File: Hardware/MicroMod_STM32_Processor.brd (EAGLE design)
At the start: 22 x 22 mm, 47 parts, among them J1 MICROMOD-2222, U1 STM32F405RGT6, U3 W25QXX128MBIT-6X5, Y1 12MHz, Y2 32.768kHz

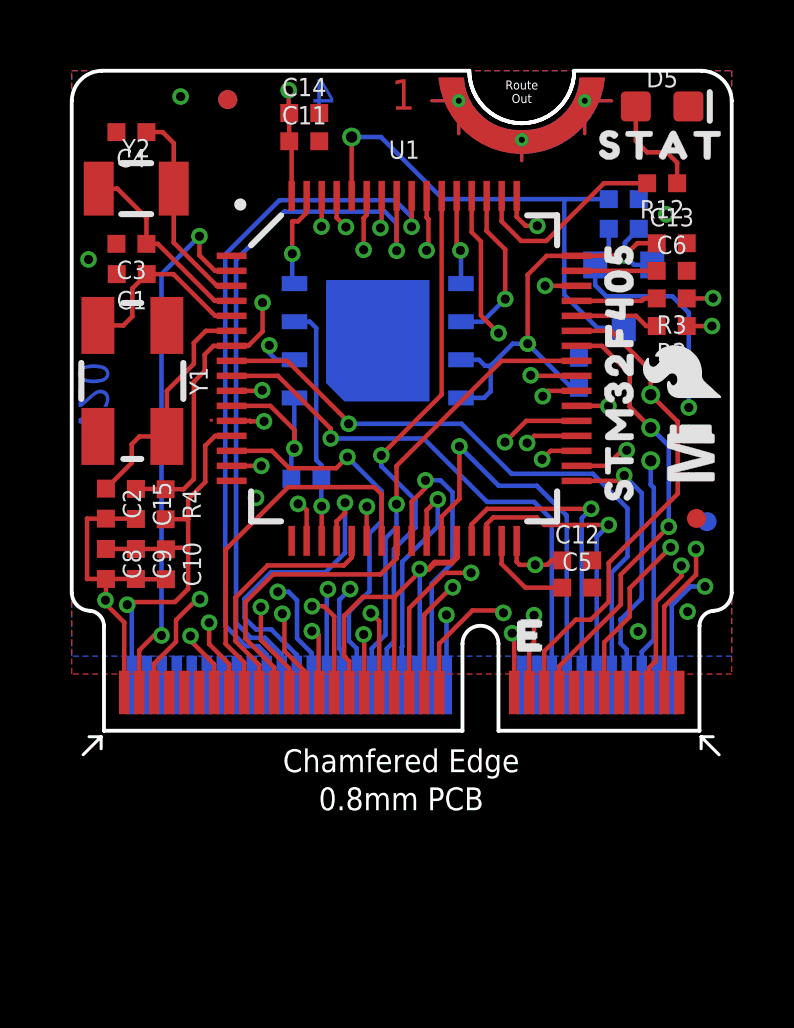
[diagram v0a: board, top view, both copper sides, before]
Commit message: Move some vias, replace STM32 with library part.
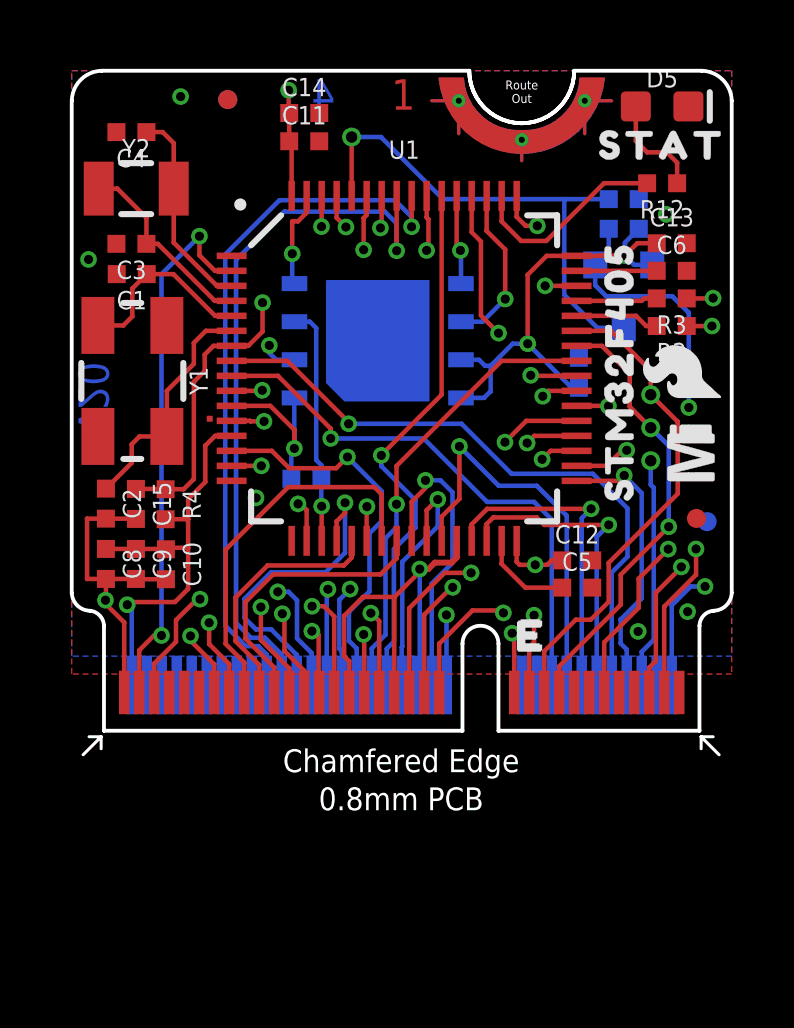
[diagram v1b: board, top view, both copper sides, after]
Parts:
- U1: device STM32_Temp:TQFP64 -> SparkFun-IC-Microcontroller:TQFP64
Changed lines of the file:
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@@
 <dimension x1="0" y1="21" x2="22" y2="21" x3="11" y3="26" textsize="1.27" textratio="15" layer="47" visible="yes"/>
 <text x="-3.454" y="-16.074" size="1.778" layer="51" font="vector">Revised by: Alex Brudner</text>
-<rectangle x1="4.6" y1="10.3" x2="4.7" y2="10.4" layer="1"/>
+<rectangle x1="4.5" y1="10.3" x2="4.7" y2="10.5" layer="1"/>
 <rectangle x1="7" y1="6.3" x2="7.1" y2="6.4" layer="41"/>
 <rectangle x1="6.9" y1="7.1" x2="7" y2="7.5" layer="41"/>
@@
 <attribute name="VALUE" x="2.568" y="7.55" size="0.6096" layer="27" font="vector" ratio="20" rot="R270" align="top-center"/>
 </element>
-<element name="U1" library="STM32_Temp" package="TQFP64" value="STM32F405RGT6" x="11.08" y="12.08" smashed="yes" rot="R270">
+<element name="U1" library="SparkFun-IC-Microcontroller" package="TQFP64" value="STM32F405RGT6" x="11.08" y="12.08" smashed="yes" rot="R270">
 <attribute name="NAME" x="11.08" y="19.065" size="0.6096" layer="25" font="vector" ratio="20" align="bottom-center"/>
 <attribute name="PROD_ID" value="IC-11709" x="3.46" y="-32.37" size="1.778" layer="27" rot="R270" display="off"/>
@@
 <wire x1="20.569" y1="13.931" x2="20.0168" y2="14.4832" width="0.1524" layer="16"/>
 <wire x1="17.75" y1="1.275" x2="17.75" y2="2.95" width="0.1524" layer="1"/>
-<wire x1="17.75" y1="2.95" x2="18.6" y2="3.8" width="0.1524" layer="1"/>
-<wire x1="18.6" y1="3.8" x2="18.6" y2="4.74986875" width="0.1524" layer="1"/>
-<wire x1="18.6" y1="4.74986875" x2="19.96433125" y2="6.1142" width="0.1524" layer="1"/>
-<via x="19.96433125" y="6.1142" extent="1-16" drill="0.3048"/>
-<wire x1="19.96433125" y1="6.1142" x2="20.569" y2="6.71886875" width="0.1524" layer="15"/>
-<wire x1="20.569" y1="6.71886875" x2="20.569" y2="10.773" width="0.1524" layer="15"/>
+<wire x1="17.75" y1="2.95" x2="18.9" y2="4.1" width="0.1524" layer="1"/>
+<wire x1="18.9" y1="4.1" x2="18.9" y2="5.06986875" width="0.1524" layer="1"/>
+<wire x1="18.9" y1="5.06986875" x2="19.88433125" y2="6.0542" width="0.1524" layer="1"/>
+<via x="19.88433125" y="6.0542" extent="1-16" drill="0.3048"/>
+<wire x1="19.88433125" y1="6.0542" x2="20.569" y2="6.73886875" width="0.1524" layer="15"/>
+<wire x1="20.569" y1="6.73886875" x2="20.569" y2="10.773" width="0.1524" layer="15"/>
 </signal>
 <signal name="SCK">
@@
 <contactref element="R2" pad="1"/>
 <contactref element="J1" pad="5"/>
-<wire x1="19.47" y1="4.3" x2="19.47" y2="2.325" width="0.1524" layer="1"/>
+<wire x1="19.47" y1="4.6" x2="19.47" y2="2.325" width="0.1524" layer="1"/>
 <wire x1="19.25" y1="1.275" x2="19.25" y2="2.105" width="0.1524" layer="1"/>
 <wire x1="19.47" y1="2.325" x2="19.25" y2="2.105" width="0.1524" layer="1"/>
-<wire x1="20.32" y1="5.15" x2="20.32" y2="5.5" width="0.1524" layer="1"/>
-<wire x1="20.32" y1="5.15" x2="19.47" y2="4.3" width="0.1524" layer="1"/>
-<via x="20.32" y="5.5" extent="1-16" drill="0.3048"/>
-<wire x1="21.020425" y1="5.502" x2="21.458" y2="5.939575" width="0.1524" layer="2"/>
-<wire x1="21.020425" y1="5.502" x2="20.322" y2="5.502" width="0.1524" layer="2"/>
-<wire x1="20.32" y1="5.5" x2="20.322" y2="5.502" width="0.1524" layer="2"/>
+<wire x1="20.32" y1="5.45" x2="20.32" y2="5.46" width="0.1524" layer="1"/>
+<wire x1="20.32" y1="5.45" x2="19.47" y2="4.6" width="0.1524" layer="1"/>
+<via x="20.32" y="5.46" extent="1-16" drill="0.3048"/>
+<wire x1="20.980425" y1="5.462" x2="21.458" y2="5.939575" width="0.1524" layer="2"/>
+<wire x1="20.980425" y1="5.462" x2="20.322" y2="5.462" width="0.1524" layer="2"/>
+<wire x1="20.32" y1="5.46" x2="20.322" y2="5.462" width="0.1524" layer="2"/>
 <via x="21.34" y="13.49" extent="1-16" drill="0.3048"/>
 <wire x1="21.34" y1="13.49" x2="20.5" y2="13.49" width="0.1524" layer="1"/>

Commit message: Ready for v11 protos.
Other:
- board text added: "Board Thickness is 0.8mm 4-Layer Beveled Edge ENIG finish"
- board text added: "v11"
- board text removed: "0.8mm PCB ENIG finish 45 degree chamfered edge Four layer design"
- board text removed: "v20"
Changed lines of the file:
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@@
 <drawing>
 <settings>
-<setting alwaysvectorfont="yes"/>
+<setting alwaysvectorfont="no"/>
 <setting verticaltext="up"/>
 </settings>
@@
 <wire x1="0" y1="21" x2="1" y2="22" width="0.127" layer="20" curve="-87.205638"/>
 <wire x1="16.75" y1="22" x2="13.25" y2="22" width="0.127" layer="20" curve="-180"/>
-<text x="0.221" y="9.961" size="1.016" layer="16" font="vector" ratio="15" rot="SMR90">v20</text>
+<text x="0.221" y="9.961" size="1.016" layer="16" font="vector" ratio="15" rot="SMR90">v11</text>
 <text x="11.84" y="-12.98" size="1.778" layer="51" font="vector">Alex Wende</text>
-<text x="39" y="28" size="1.778" layer="51" font="vector" ratio="15">0.8mm PCB
-ENIG finish
-45 degree chamfered edge
-Four layer design</text>
+<text x="38.7" y="28.9" size="1.778" layer="51" font="vector" ratio="15">Board Thickness is 0.8mm
+4-Layer
+Beveled Edge
+ENIG finish</text>
 <text x="11.049" y="21.209" size="1.016" layer="1" font="vector" ratio="15" align="center">1</text>
 <text x="10.033" y="21.209" size="1.016" layer="2" font="vector" ratio="15" align="center">2</text>
@@
 <dimension x1="0" y1="21" x2="22" y2="21" x3="11" y3="26" textsize="1.27" textratio="15" layer="47" visible="yes"/>
 <text x="-3.454" y="-16.074" size="1.778" layer="51" font="vector">Revised by: Alex Brudner</text>
-<rectangle x1="4.5" y1="10.3" x2="4.7" y2="10.5" layer="1"/>
+<rectangle x1="4.5" y1="10.3" x2="4.7" y2="10.5" layer="41"/>
 <rectangle x1="7" y1="6.3" x2="7.1" y2="6.4" layer="41"/>
 <rectangle x1="6.9" y1="7.1" x2="7" y2="7.5" layer="41"/>
+<text x="39" y="31" size="1.778" layer="51" font="vector" ratio="15"></text>
+<text x="39" y="28" size="1.778" layer="51" font="vector" ratio="15"></text>
 </plain>
 <attributes>
@@
 <wire x1="16.83" y1="8.33" x2="18.236" y2="8.33" width="0.1524" layer="1"/>
 <contactref element="J1" pad="8"/>
-<wire x1="18.415" y1="8.509" x2="18.996" y2="7.928" width="0.1524" layer="16"/>
-<wire x1="18.996" y1="4.41" x2="18.996" y2="7.928" width="0.1524" layer="16"/>
+<wire x1="18.415" y1="8.509" x2="18.896" y2="8.028" width="0.1524" layer="16"/>
+<wire x1="18.896" y1="4.41" x2="18.896" y2="8.028" width="0.1524" layer="16"/>
 <wire x1="18.5" y1="1.525" x2="18.5" y2="2.7075" width="0.1524" layer="16"/>
 <wire x1="18.5" y1="2.7075" x2="18.2974" y2="2.9101" width="0.1524" layer="16"/>
-<wire x1="18.2974" y1="2.9101" x2="18.2974" y2="3.7114" width="0.1524" layer="16"/>
-<wire x1="18.2974" y1="3.7114" x2="18.996" y2="4.41" width="0.1524" layer="16"/>
+<wire x1="18.2974" y1="2.9101" x2="18.2974" y2="3.8114" width="0.1524" layer="16"/>
+<wire x1="18.2974" y1="3.8114" x2="18.896" y2="4.41" width="0.1524" layer="16"/>
 </signal>
 <signal name="FLASH_SCK">
@@
 <contactref element="J1" pad="73"/>
 <via x="2.9926" y="3.175" extent="1-16" drill="0.3048"/>
-<wire x1="2.9926" y1="3.175" x2="2.7426" y2="3.175" width="0.1524" layer="1"/>
-<wire x1="2.7426" y1="3.175" x2="2.25" y2="2.6824" width="0.1524" layer="1"/>
-<wire x1="2.25" y1="2.6824" x2="2.25" y2="1.275" width="0.1524" layer="1"/>
+<wire x1="2.9926" y1="3.175" x2="2.5426" y2="3.175" width="0.1524" layer="1"/>
+<wire x1="2.5426" y1="3.175" x2="2.25" y2="2.8824" width="0.1524" layer="1"/>
+<wire x1="2.25" y1="2.8824" x2="2.25" y2="1.275" width="0.1524" layer="1"/>
 <contactref element="U1" pad="2"/>
 <wire x1="2.9926" y1="3.175" x2="2.9926" y2="15.2196" width="0.1524" layer="16"/>
@@
 <wire x1="3.13" y1="8.05" x2="3.73" y2="8.05" width="0.1524" layer="1"/>
 <wire x1="4.07" y1="8.39" x2="3.73" y2="8.05" width="0.1524" layer="1"/>
-<wire x1="19.4" y1="8.1" x2="19.3" y2="8.2" width="0.1524" layer="16"/>
-<wire x1="19.3" y1="9" x2="19.3" y2="8.2" width="0.1524" layer="16"/>
-<wire x1="19.4" y1="8.1" x2="19.4" y2="3.03" width="0.1524" layer="16"/>
-<wire x1="19.4" y1="3.03" x2="19" y2="2.63" width="0.1524" layer="16"/>
+<wire x1="19.3" y1="9" x2="19.3" y2="2.93" width="0.1524" layer="16"/>
+<wire x1="19.3" y1="2.93" x2="19" y2="2.63" width="0.1524" layer="16"/>
 <wire x1="19" y1="2.63" x2="19" y2="1.525" width="0.1524" layer="16"/>
 <wire x1="5.33" y1="12.83" x2="5.883" y2="12.83" width="0.1524" layer="1"/>
@@
 <contactref element="J1" pad="14"/>
 <contactref element="U1" pad="29"/>
-<wire x1="17.31273125" y1="7.3974" x2="17" y2="7.08466875" width="0.1524" layer="16"/>
-<wire x1="17" y1="7.08466875" x2="17" y2="1.525" width="0.1524" layer="16"/>
+<wire x1="17.31273125" y1="7.3974" x2="17.31273125" y2="6.8974" width="0.1524" layer="16"/>
+<wire x1="17.31273125" y1="6.8974" x2="17" y2="6.58466875" width="0.1524" layer="16"/>
+<wire x1="17" y1="6.58466875" x2="17" y2="1.525" width="0.1524" layer="16"/>
 <via x="17.31273125" y="7.3974" extent="1-16" drill="0.3048"/>
 <wire x1="17.31273125" y1="7.3974" x2="13.8474" y2="7.3974" width="0.1524" layer="1"/>
@@
 <signal name="D0">
 <contactref element="J1" pad="10"/>
-<wire x1="18.523" y1="7.413" x2="17.3712" y2="8.5648" width="0.1524" layer="16"/>
-<wire x1="18.523" y1="7.413" x2="18.523" y2="5.799" width="0.1524" layer="16"/>
-<wire x1="18" y1="5.276" x2="18.523" y2="5.799" width="0.1524" layer="16"/>
-<wire x1="18" y1="5.276" x2="18" y2="1.525" width="0.1524" layer="16"/>
+<wire x1="18.523" y1="7.313" x2="17.2712" y2="8.5648" width="0.1524" layer="16"/>
+<wire x1="18.523" y1="7.313" x2="18.523" y2="4.799" width="0.1524" layer="16"/>
+<wire x1="18" y1="4.276" x2="18.523" y2="4.799" width="0.1524" layer="16"/>
+<wire x1="18" y1="4.276" x2="18" y2="1.525" width="0.1524" layer="16"/>
 <via x="9.231" y="10.232" extent="1-16" drill="0.3048"/>
 <contactref element="U1" pad="8"/>
-<wire x1="17.3712" y1="8.5648" x2="14.6611" y2="8.5648" width="0.1524" layer="16"/>
+<wire x1="17.2712" y1="8.5648" x2="14.6611" y2="8.5648" width="0.1524" layer="16"/>
 <wire x1="12.9939" y1="10.232" x2="9.231" y2="10.232" width="0.1524" layer="16"/>
 <wire x1="14.6611" y1="8.5648" x2="12.9939" y2="10.232" width="0.1524" layer="16"/>
@@
 <contactref element="U1" pad="17"/>
 <via x="6.1442" y="7.7626" extent="1-16" drill="0.3048"/>
-<via x="18.88" y="3.31" extent="1-16" drill="0.3048"/>
+<via x="18.78" y="3.21" extent="1-16" drill="0.3048"/>
 </signal>
 <signal name="3.3V">
@@
 <wire x1="3.14" y1="6.1" x2="3.88" y2="6.1" width="0.1524" layer="1"/>
 <wire x1="13.745" y1="11.095" x2="12.975" y2="11.095" width="0.1524" layer="16"/>
-<wire x1="16.906" y1="11.433" x2="16.667" y2="11.433" width="0.1524" layer="16"/>
+<wire x1="16.906" y1="11.433" x2="16.267" y2="11.433" width="0.1524" layer="16"/>
 <wire x1="15.2" y1="12.9" x2="14.7" y2="12.9" width="0.1524" layer="16"/>
 <wire x1="14.7" y1="12.9" x2="13.965" y2="12.165" width="0.1524" layer="16"/>
@@
 <wire x1="13.775" y1="12.165" x2="13.575" y2="12.365" width="0.1524" layer="16"/>
 <wire x1="13.575" y1="12.365" x2="12.975" y2="12.365" width="0.1524" layer="16"/>
-<wire x1="16.667" y1="11.433" x2="15.2" y2="12.9" width="0.1524" layer="16"/>
+<wire x1="16.267" y1="11.433" x2="16" y2="11.7" width="0.1524" layer="16"/>
+<wire x1="16" y1="12.5" x2="15.6" y2="12.9" width="0.1524" layer="16"/>
+<wire x1="15.6" y1="12.9" x2="15.2" y2="12.9" width="0.1524" layer="16"/>
+<wire x1="16" y1="12.5" x2="16" y2="11.7" width="0.1524" layer="16"/>
 <wire x1="13.965" y1="12.165" x2="13.965" y2="11.315" width="0.1524" layer="16"/>
 <wire x1="13.965" y1="11.315" x2="13.745" y2="11.095" width="0.1524" layer="16"/>

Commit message: Update for v20 pushing to reds.
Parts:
- removed TP1, TP2, TP3, TP4: TEST-POINTTP_15TH_THRU, SparkFun-Connectors:TP_15TH
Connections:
- net !RESET: no longer TP4.1
- net BOOT0: no longer TP3.1
- net RX1: no longer TP1.1
- net TX1: no longer TP2.1
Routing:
- net BOOT0: track 17.0 -> 16.5 mm, vias 0 -> 1
- net !RESET: track 37.3 -> 37.2 mm, vias 1 -> 2
- net TX1: vias 1 -> 2
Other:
- board text added: "v20"
- board text removed: "v11"
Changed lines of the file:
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@@
 <drawing>
 <settings>
-<setting alwaysvectorfont="no"/>
+<setting alwaysvectorfont="yes"/>
 <setting verticaltext="up"/>
 </settings>
@@
 <wire x1="0" y1="21" x2="1" y2="22" width="0.127" layer="20" curve="-87.205638"/>
 <wire x1="16.75" y1="22" x2="13.25" y2="22" width="0.127" layer="20" curve="-180"/>
-<text x="0.221" y="9.961" size="1.016" layer="16" font="vector" ratio="15" rot="SMR90">v11</text>
+<text x="0.221" y="9.961" size="1.016" layer="16" font="vector" ratio="15" rot="SMR90">v20</text>
 <text x="11.84" y="-12.98" size="1.778" layer="51" font="vector">Alex Wende</text>
 <text x="38.7" y="28.9" size="1.778" layer="51" font="vector" ratio="15">Board Thickness is 0.8mm
@@
 <element name="U$6" library="SparkFun-Aesthetics" package="SFE_LOGO_FLAME_.1" value="" x="20.32" y="11.95" smashed="yes" rot="R90"/>
 <element name="U$7" library="SparkFun-Aesthetics" package="PRODUCTION_INSTRUCTIONS" value="" x="37" y="49" smashed="yes"/>
-<element name="TP1" library="SparkFun-Connectors" package="TP_15TH" value="TEST-POINTTP_15TH_THRU" x="19.3" y="11.2" smashed="yes" rot="MR0"/>
-<element name="TP2" library="SparkFun-Connectors" package="TP_15TH" value="TEST-POINTTP_15TH_THRU" x="19.3" y="10.1" smashed="yes" rot="MR0"/>
-<element name="TP3" library="SparkFun-Connectors" package="TP_15TH" value="TEST-POINTTP_15TH_THRU" x="9.33" y="19.79" smashed="yes" rot="MR0"/>
-<element name="TP4" library="SparkFun-Connectors" package="TP_15TH" value="TEST-POINTTP_15TH_THRU" x="19.3" y="9" smashed="yes" rot="MR0"/>
 </elements>
 <signals>
@@
 <wire x1="3.13" y1="8.05" x2="3.73" y2="8.05" width="0.1524" layer="1"/>
 <wire x1="4.07" y1="8.39" x2="3.73" y2="8.05" width="0.1524" layer="1"/>
-<wire x1="19.3" y1="9" x2="19.3" y2="2.93" width="0.1524" layer="16"/>
-<wire x1="19.3" y1="2.93" x2="19" y2="2.63" width="0.1524" layer="16"/>
-<wire x1="19" y1="2.63" x2="19" y2="1.525" width="0.1524" layer="16"/>
+<wire x1="19" y1="1.525" x2="19" y2="2.63" width="0.1524" layer="16"/>
 <wire x1="5.33" y1="12.83" x2="5.883" y2="12.83" width="0.1524" layer="1"/>
 <wire x1="5.883" y1="12.83" x2="6.36" y2="13.307" width="0.1524" layer="1"/>
@@
 <wire x1="14.171575" y1="15.7" x2="12.741575" y2="14.27" width="0.1524" layer="2"/>
 <wire x1="6.36" y1="14.27" x2="12.741575" y2="14.27" width="0.1524" layer="2"/>
-<contactref element="TP4" pad="1"/>
 <wire x1="18.568" y1="15.332" x2="16.329575" y2="15.332" width="0.1524" layer="2"/>
 <wire x1="15.961575" y1="15.7" x2="14.171575" y2="15.7" width="0.1524" layer="2"/>
 <wire x1="16.329575" y1="15.332" x2="15.961575" y2="15.7" width="0.1524" layer="2"/>
-<wire x1="18.568" y1="15.332" x2="19.9" y2="14" width="0.1524" layer="2"/>
-<wire x1="19.9" y1="9.6" x2="19.3" y2="9" width="0.1524" layer="2"/>
-<wire x1="19.9" y1="14" x2="19.9" y2="9.6" width="0.1524" layer="2"/>
+<wire x1="19.8" y1="14.1" x2="18.568" y2="15.332" width="0.1524" layer="2"/>
+<wire x1="19.3" y1="2.93" x2="19.3" y2="9.3" width="0.1524" layer="16"/>
+<via x="19.3" y="9.3" extent="1-16" drill="0.3048"/>
+<wire x1="19.3" y1="9.3" x2="19.8" y2="9.8" width="0.1524" layer="2"/>
+<wire x1="19" y1="2.63" x2="19.3" y2="2.93" width="0.1524" layer="16"/>
+<wire x1="19.8" y1="9.8" x2="19.8" y2="14.1" width="0.1524" layer="2"/>
 </signal>
 <signal name="BOOT0">
@@
 <wire x1="17.518" y1="13.43" x2="18.4" y2="13.43" width="0.1524" layer="16"/>
 <wire x1="16.42" y1="14.528" x2="17.518" y2="13.43" width="0.1524" layer="16"/>
-<wire x1="10.309" y1="19.79" x2="12.379" y2="17.72" width="0.1524" layer="16"/>
+<wire x1="12.379" y1="17.72" x2="10.6995" y2="19.3995" width="0.1524" layer="16"/>
 <wire x1="16.42" y1="17.72" x2="17.9" y2="17.72" width="0.1524" layer="16"/>
 <wire x1="16.42" y1="17.72" x2="12.379" y2="17.72" width="0.1524" layer="16"/>
-<contactref element="TP3" pad="1"/>
-<wire x1="9.33" y1="17.83" x2="9.33" y2="19.79" width="0.1524" layer="1"/>
-<wire x1="9.33" y1="19.79" x2="10.309" y2="19.79" width="0.1524" layer="16"/>
+<wire x1="9.33" y1="17.83" x2="9.33" y2="19.4" width="0.1524" layer="1"/>
+<via x="9.33" y="19.4" extent="1-16" drill="0.3048"/>
+<wire x1="9.33" y1="19.4" x2="10.699" y2="19.4" width="0.1524" layer="16"/>
+<wire x1="10.699" y1="19.4" x2="10.6995" y2="19.3995" width="0.1524" layer="16"/>
 </signal>
 <signal name="N$45">
@@
 <contactref element="J1" pad="17"/>
 <contactref element="U1" pad="42"/>
-<contactref element="TP2" pad="1"/>
-<wire x1="16.83" y1="12.83" x2="17.67" y2="12.83" width="0.1524" layer="1"/>
-<wire x1="18.6" y1="10.8" x2="19.3" y2="10.1" width="0.1524" layer="1"/>
-<wire x1="17.67" y1="12.83" x2="18.6" y2="11.9" width="0.1524" layer="1"/>
-<wire x1="18.6" y1="11.9" x2="18.6" y2="10.8" width="0.1524" layer="1"/>
+<wire x1="16.83" y1="12.83" x2="17.57" y2="12.83" width="0.1524" layer="1"/>
+<wire x1="17.57" y1="12.83" x2="19.2" y2="11.2" width="0.1524" layer="1"/>
+<wire x1="19.2" y1="11.2" x2="19.2" y2="10.2" width="0.1524" layer="1"/>
 <wire x1="16.25" y1="1.275" x2="16.25" y2="2.15" width="0.1524" layer="1"/>
 <wire x1="18.3" y1="4.2" x2="18.3" y2="5.2" width="0.1524" layer="1"/>
 <wire x1="16.25" y1="2.15" x2="18.3" y2="4.2" width="0.1524" layer="1"/>
-<wire x1="19.3" y1="10.1" x2="19.9" y2="9.5" width="0.1524" layer="16"/>
 <wire x1="19.9" y1="9.5" x2="19.9" y2="6.8" width="0.1524" layer="16"/>
 <via x="19.9" y="6.8" extent="1-16" drill="0.3048"/>
 <wire x1="19.9" y1="6.8" x2="18.3" y2="5.2" width="0.1524" layer="1"/>
+<via x="19.2" y="10.2" extent="1-16" drill="0.3048"/>
+<wire x1="19.2" y1="10.2" x2="19.9" y2="9.5" width="0.1524" layer="16"/>
 </signal>
 <signal name="RX1">
 <contactref element="J1" pad="19"/>
 <contactref element="U1" pad="43"/>
-<contactref element="TP1" pad="1"/>
-<wire x1="19.3" y1="11.2" x2="19.3" y2="12" width="0.1524" layer="1"/>
-<wire x1="19.3" y1="12" x2="17.97" y2="13.33" width="0.1524" layer="1"/>
 <wire x1="17.97" y1="13.33" x2="16.83" y2="13.33" width="0.1524" layer="1"/>
 <wire x1="15.75" y1="1.275" x2="15.75" y2="2.65" width="0.1524" layer="1"/>
-<wire x1="20.2" y1="7.9" x2="20.2" y2="10.3" width="0.1524" layer="1"/>
-<wire x1="20.2" y1="10.3" x2="19.3" y2="11.2" width="0.1524" layer="1"/>
 <wire x1="15.75" y1="2.65" x2="16.8" y2="3.7" width="0.1524" layer="1"/>
 <wire x1="16.8" y1="3.7" x2="17.3" y2="3.7" width="0.1524" layer="1"/>
 <wire x1="17.3" y1="3.7" x2="17.9" y2="4.3" width="0.1524" layer="1"/>
 <wire x1="17.9" y1="4.3" x2="17.9" y2="5.6" width="0.1524" layer="1"/>
-<wire x1="17.9" y1="5.6" x2="20.2" y2="7.9" width="0.1524" layer="1"/>
+<wire x1="17.9" y1="5.6" x2="20.0864" y2="7.7864" width="0.1524" layer="1"/>
+<wire x1="20.0864" y1="7.7864" x2="20.0864" y2="11.2136" width="0.1524" layer="1"/>
+<wire x1="20.0864" y1="11.2136" x2="17.97" y2="13.33" width="0.1524" layer="1"/>
 </signal>
 <signal name="AUD_OUT">
@@
 <via x="7.23" y="21.35" extent="1-16" drill="0.3048"/>
 <via x="15.45" y="5.53" extent="1-16" drill="0.3048"/>
-<wire x1="15.45" y1="5.53" x2="14.93" y2="5.53" width="0.1524" layer="1"/>
-<wire x1="14.93" y1="5.53" x2="14.83" y2="5.63" width="0.1524" layer="1"/>
-<wire x1="14.83" y1="6.33" x2="14.83" y2="5.63" width="0.1524" layer="1"/>
+<wire x1="15.45" y1="5.53" x2="15.03" y2="5.53" width="0.1524" layer="1"/>
+<wire x1="15.03" y1="5.53" x2="14.83" y2="5.73" width="0.1524" layer="1"/>
+<wire x1="14.83" y1="6.33" x2="14.83" y2="5.73" width="0.1524" layer="1"/>
 <wire x1="16.35" y1="5.68" x2="16" y2="5.68" width="0.1524" layer="1"/>
 <wire x1="16" y1="5.68" x2="15.85" y2="5.53" width="0.1524" layer="1"/>
